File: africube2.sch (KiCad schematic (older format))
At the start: 25 parts, among them J1 SMA Edge FM, J2 Conn_01x04, J3 RPi_GPIO, U1 TQP7M9105, U2 SXBP-150+, U3 BA178M05FP-E2

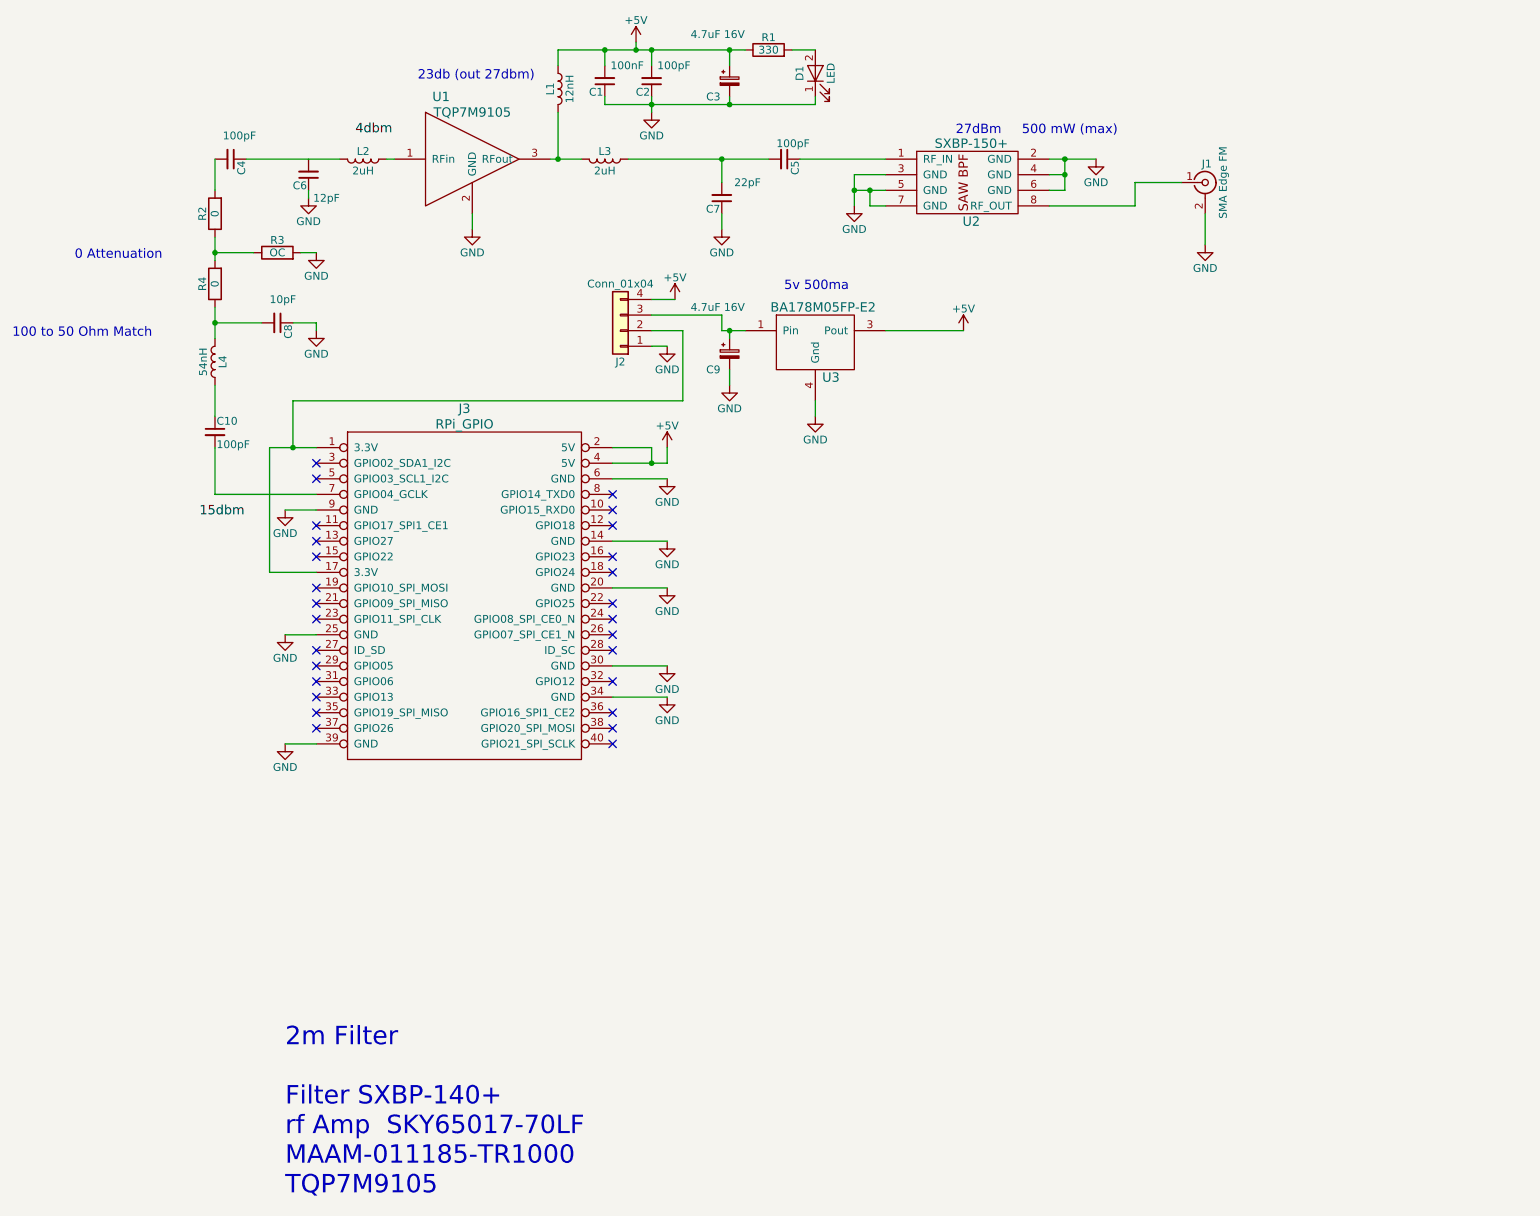
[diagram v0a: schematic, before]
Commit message: adding directional copler
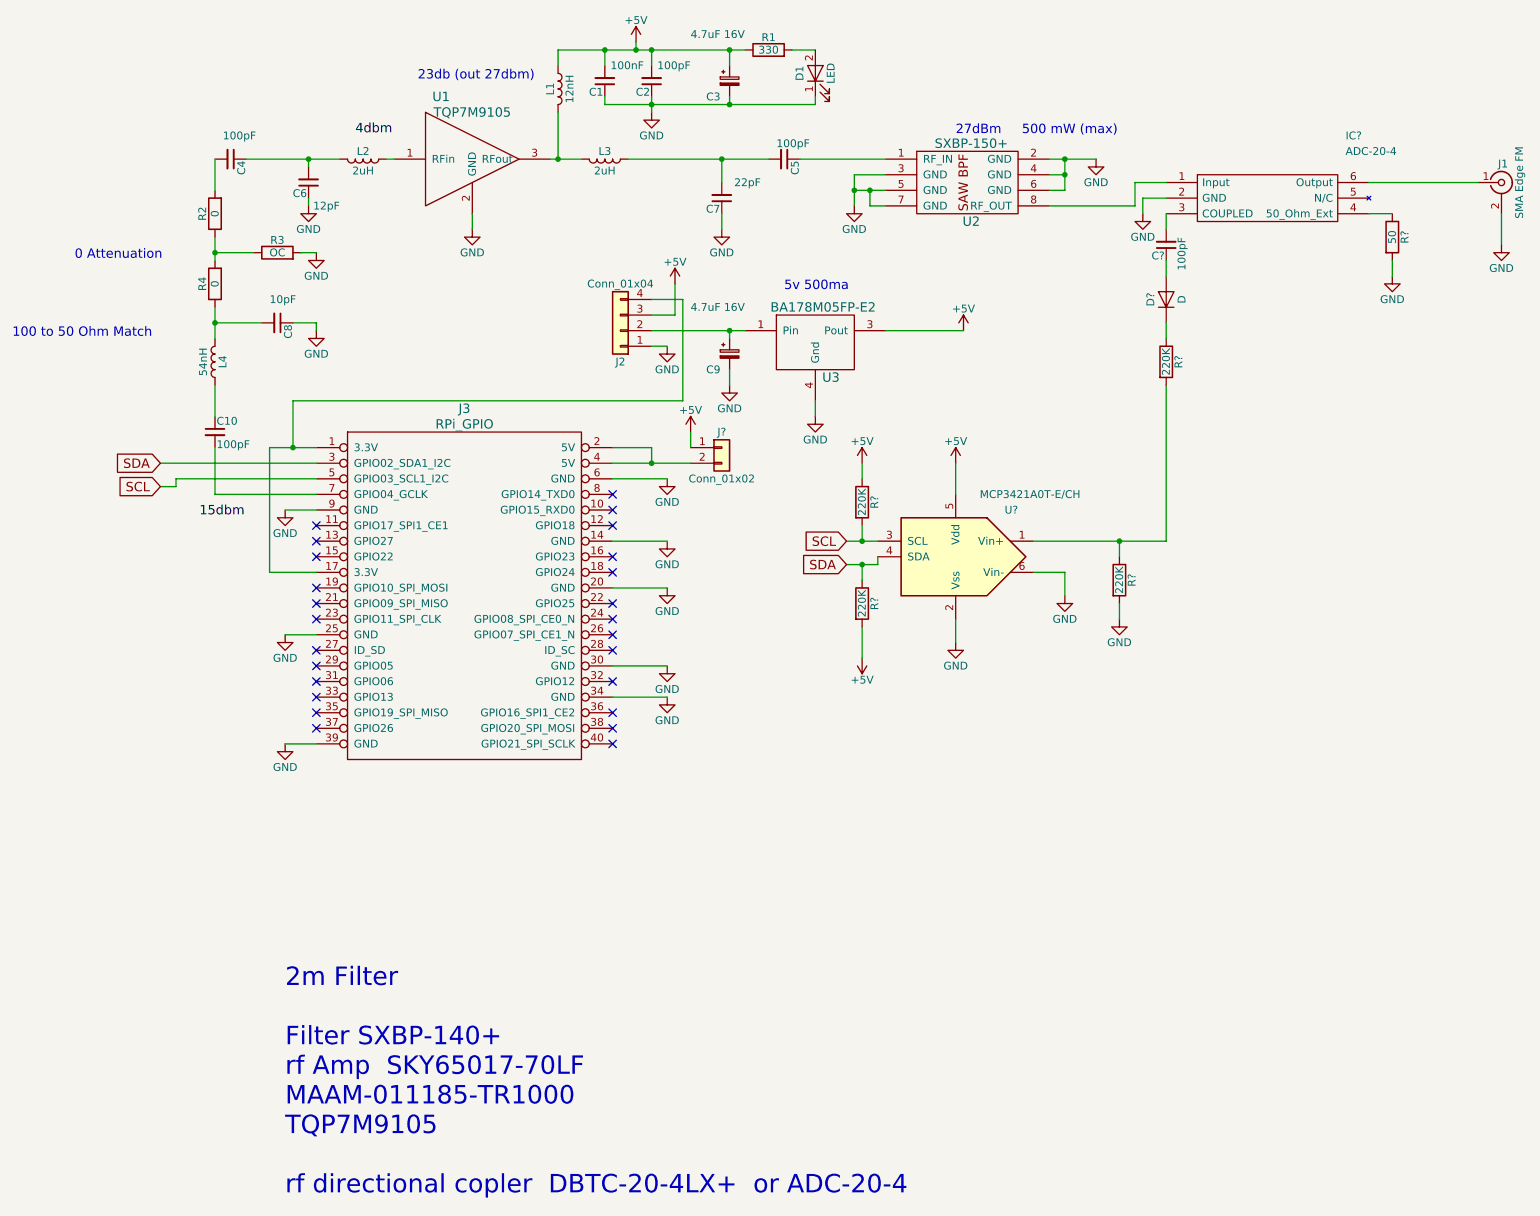
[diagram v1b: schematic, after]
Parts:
- added C?: 100pF, Capacitors_SMD:C_0805_HandSoldering, symbol C_Small
- added D?: D, symbol D
- added IC?: ADC-20-4, ADC-20-4+, symbol ADC-20-4
- added J?: Conn_01x02, symbol Conn_01x02
- added R? (x4): 220K, Resistors_SMD:R_0805_HandSoldering, symbol R
- added R?: 50, Resistors_SMD:R_0805_HandSoldering, symbol R
- added U?: MCP3421A0T-E/CH, symbol MCP3421A0T-E/CH
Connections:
- net +5V: now also J2.3 (Pin_3), J?.1 (Pin_1), R?.1, R?.2, U?.5 (Vdd); no longer J2.4 (Pin_4), J3.2 (5V), J3.4 (5V)
- net GND: now also IC?.2 (GND), R?.2, R?.2, U?.2 (Vss), U?.6 (Vin-)
- net at J1.1 (In): now also IC?.6 (Output); no longer U2.8 (RF_OUT)
- net at J3.1 (3.3V), J3.17 (3.3V): now also J2.4 (Pin_4); no longer J2.2 (Pin_2)
- net SDA: now reaches J3.3 (GPIO02_SDA1_I2C)
- net SDA: now also R?.1, U?.4 (SDA)
- net SCL: now reaches J3.5 (GPIO03_SCL1_I2C)
- net SCL: now also R?.2, U?.3 (SCL)
- net at C4.1, L2.2: now also C6.2
- net at C9.1, U3.1 (Pin): now also J2.2 (Pin_2); no longer J2.3 (Pin_3)
- new net: J3.2 (5V), J3.4 (5V), J?.2 (Pin_2)
- new net: IC?.1 (Input), U2.8 (RF_OUT)
- new net: D?.1 (K), R?.1
- new net: C?.1, D?.2 (A)
- new net: C?.2, IC?.3 (COUPLED)
- new net: R?.1, R?.2, U?.1 (Vin+)
- new net: IC?.4 (50_Ohm_Ext), R?.1
- no-connect marks 27 -> 25
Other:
- note added: "2m Filter\n\nFilter SXBP-140+\nrf Amp SKY65017-70LF\nMAAM-011185-TR1000 \nTQP7M9105\n\nrf directional copler DBTC-20-4LX+ or ADC-20-4"
- note removed: "2m Filter\n\nFilter SXBP-140+\nrf Amp SKY65017-70LF\nMAAM-011185-TR1000 \nTQP7M9105"
- moved on the sheet: C6, J1
